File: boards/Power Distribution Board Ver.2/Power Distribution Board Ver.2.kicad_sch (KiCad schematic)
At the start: 89 parts, among them J1 Screw_Terminal_01x02, J2 Screw_Terminal_01x06, J3 Screw_Terminal_01x06, J5 Screw_Terminal_01x06, K1 Relay, K2 Relay, K3 Relay, K4 Relay, K5 Relay, K6 Relay, SW1 SW_Push_Open, U1 SIC431AED-T1-GE3, U2 SIC431AED-T1-GE3, U3 SIC431AED-T1-GE3

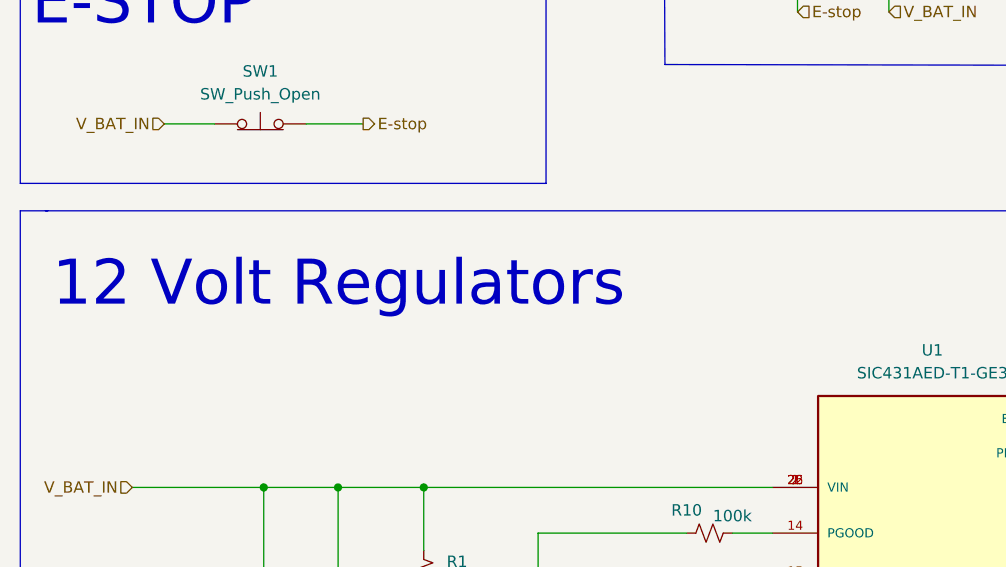
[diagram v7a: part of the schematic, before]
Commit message: Change Schematics Name
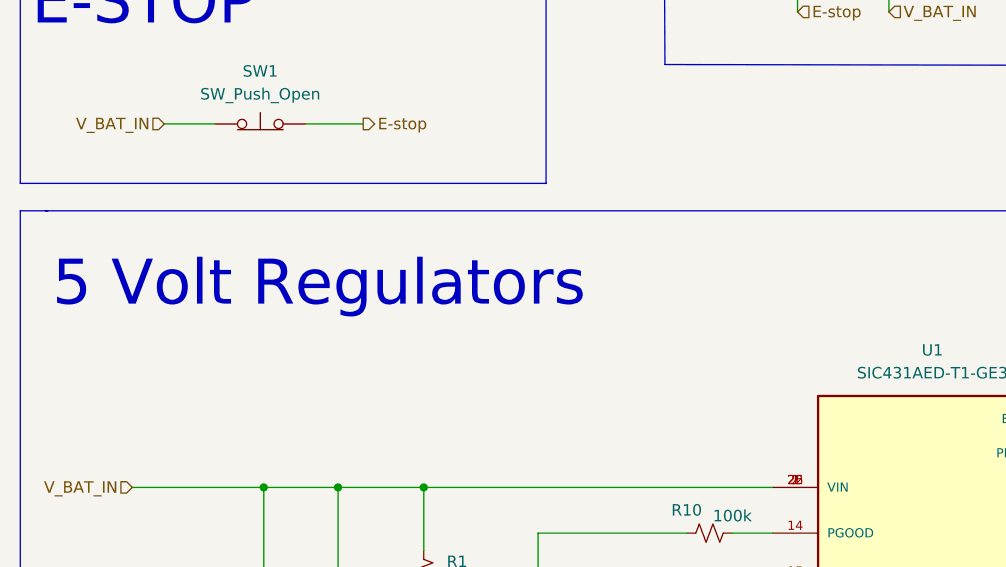
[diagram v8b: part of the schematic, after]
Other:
- note added: "5 Volt Regulators"
- note removed: "12 Volt Regulators"
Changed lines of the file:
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@@
     (effects (font (size 1.27 1.27)) (justify left bottom))
   )
-  (text "12 Volt Regulators" (at 17.526 147.828 0)
+  (text "5 Volt Regulators" (at 17.526 147.828 0)
     (effects (font (size 5 5)) (justify left bottom))
   )
